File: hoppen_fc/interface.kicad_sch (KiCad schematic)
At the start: 56 parts, among them J10 XH2.5-3P, J11 XH2.5-3P, J12 GH1.25-4P, J13 GH1.25-4P, J14 XH2.5-3P, J15 GH1.25-4P, J16 GH1.25-2P, J17 GH1.25-2P, J18 GH1.25-5P, J3 GH1.25-4P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

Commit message: work
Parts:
- removed C98: 100n, 0_resistor_smd:R_0603_1608Metric, symbol Device:C
- removed J14: XH2.5-3P, symbol 0_connectors:Conn_01x03_Mounting
- removed R54, R55, R57, R60: 47k, symbol Device:R
- added C77: 100n, 0_capacitor_smd:C_0402_1005Metric, symbol Device:C
- added J2: PH2.0-3P, 0_connectors:S3B-PH-SM4-TB-LF-SN, symbol 0_connectors:Conn_01x03_Mounting
- added R13, R14, R15, R20: 47k, 0_resistor_smd:R_0402_1005Metric, symbol Device:R
- C68, C69, C82, C83, C85, C87, C89, C91, C92, C93, C95, C96, C97: footprint 0_resistor_smd:R_0603_1608Metric -> 0_capacitor_smd:C_0402_1005Metric
- C86, C88, C90, C94: footprint (none) -> 0_capacitor_smd:CASE-B-3528-21; LCSC (none) -> C7199
- J10, J11, J6, J9: value XH2.5-3P -> PH2.0-3P; footprint (none) -> 0_connectors:S3B-PH-SM4-TB-LF-SN
- J12, J13, J15, J3, J5: footprint (none) -> 0_connectors:SM04B-GHS-TB-LF-SN
- J16, J17: footprint (none) -> 0_connectors:SM02B-GHS-TB-LF-SN
- J18: footprint (none) -> 0_connectors:SM05B-GHS-TB-LF-SN
- J7: footprint (none) -> 0_connectors:SM08B-GHS-TB-LF-SN
- J8: footprint (none) -> 0_connectors:SM06B-GHS-TB-LF-SN
- JP3, JP4: footprint (none) -> 0_misc:SolderJumper-2_P1.3mm_Bridged_RoundedPad1.0x1.5mm
- R56, R61, R62: footprint (none) -> 0_resistor_smd:R_0402_1005Metric
- U15: footprint (none) -> 0_power:SOT-23-5_L3.0-W1.7-P0.95-LS2.8-BL
- U16: footprint Package_TO_SOT_SMD:SOT-353_SC-70-5 -> 0_transceivers:SOT-23-5
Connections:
- net +3V3: now also C97.1
- net +5V_EXT: now also J11.1 (Pin_1)
- net +BAT: now also C77.1, J2.1 (Pin_1); no longer C89.1, J11.1 (Pin_1)
- net CAM_PWR: now also C89.1; no longer C97.1
- net EXT_LED_D_5V: now also J11.2 (Pin_2)
- net GND: now also C77.2, J2.3 (Pin_3), J2.MP1, J2.MP2, R13.2, R14.2, R15.2, R20.2
- net PWM2: now also J2.2 (Pin_2), R15.1; no longer J9.2 (Pin_2)
- net PWM3: now also J9.2 (Pin_2), R14.1; no longer J10.2 (Pin_2)
- net PWM4: now also J10.2 (Pin_2), R13.1; no longer J11.2 (Pin_2)
- net at U15.3 (RSET): now also R20.1

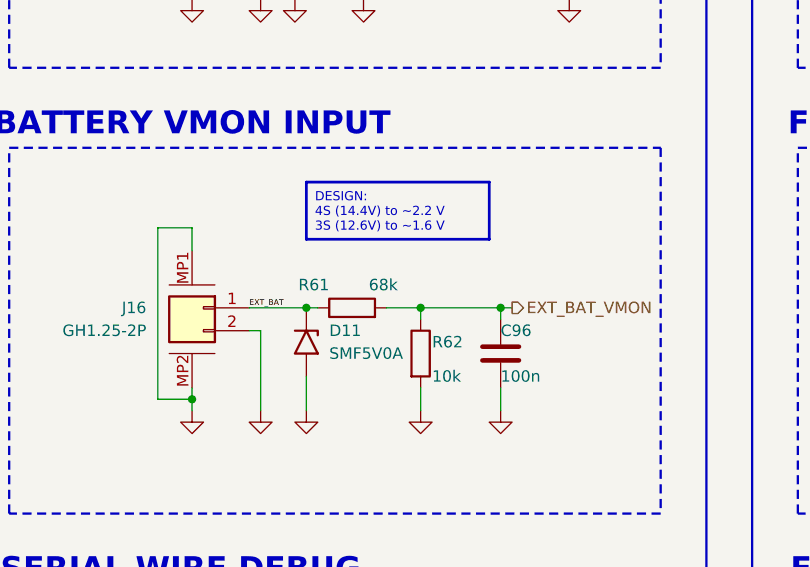
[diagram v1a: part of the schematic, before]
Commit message: power input/generation reworked
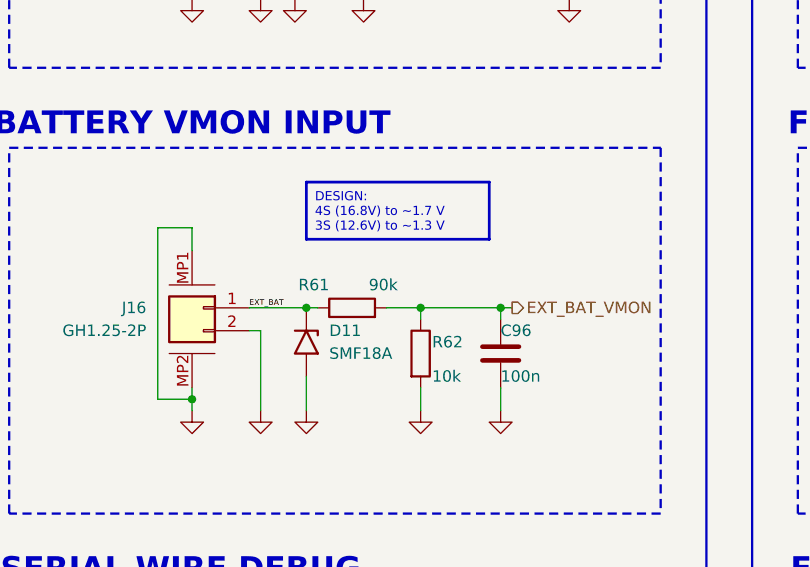
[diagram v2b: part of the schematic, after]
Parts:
- removed D11: SMF5V0A, 0_diodes:D_SMF, symbol 0_diodes:SMF5V0A
- added D11: SMF18A, Diode_SMD:D_SMF, symbol Diode:SMF18A
- C84: footprint (none) -> 0_capacitor_smd:CASE-B-3528-21; LCSC (none) -> C7199
- R61: value 68k -> 90k
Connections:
- net EXT_BAT: now also D11.1 (A1)
- net GND: now also D11.2 (A2)
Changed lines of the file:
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@@
 		)
 	)
-	(text_box "DESIGN:\n4S (14.4V) to ~2.2 V\n3S (12.6V) to ~1.6 V"
+	(text_box "DESIGN:\n4S (16.8V) to ~1.7 V\n3S (12.6V) to ~1.3 V"
 		(exclude_from_sim no)
 		(at 247.65 104.14 0)
@@
 	)
 	(junction
-		(at 247.65 118.11)
-		(diameter 0)
-		(color 0 0 0 0)
-	)
-	(junction
 		(at 148.59 133.35)
 		(diameter 0)
@@
 	)
 	(junction
+		(at 247.65 118.11)
+		(diameter 0)
+		(color 0 0 0 0)
+	)
+	(junction
 		(at 246.38 217.17)
 		(diameter 0)
@@
 	(wire
 		(pts
-			(xy 241.3 118.11) (xy 247.65 118.11)
-		)
-		(stroke
-			(width 0)
-			(type default)
-		)
-	)
-	(wire
-		(pts
 			(xy 242.57 207.01) (xy 242.57 219.71)
 		)
@@
 	(wire
 		(pts
+			(xy 247.65 118.11) (xy 248.92 118.11)
+		)
+		(stroke
+			(width 0)
+			(type default)
+		)
+	)
+	(wire
+		(pts
 			(xy 330.2 168.91) (xy 330.2 158.75)
 		)
@@
 	(wire
 		(pts
-			(xy 247.65 118.11) (xy 248.92 118.11)
+			(xy 241.3 118.11) (xy 247.65 118.11)
 		)
 		(stroke
@@
 			)
 		)
-		(property "Value" "68k"
+		(property "Value" "90k"
 			(at 257.81 115.57 90)
 			(effects
@@
 	)
 	(symbol
-		(lib_id "power:GND")
-		(at 167.64 134.62 0)
+		(lib_id "Diode:SMF18A")
+		(at 247.65 121.92 270)
 		(unit 1)
 		(exclude_from_sim no)
@@
 		(dnp no)
 		(fields_autoplaced yes)
-		(property "Reference" "#PWR0174"
-			(at 167.64 140.97 0)
+		(property "Reference" "D11"
+			(at 250.19 120.6499 90)
 			(effects
 				(font
 					(size 1.27 1.27)
 				)
-				(hide yes)
+				(justify left)
 			)
 		)
-		(property "Value" "GND"
-			(at 167.64 139.7 0)
+		(property "Value" "SMF18A"
+			(at 250.19 123.1899 90)
 			(effects
 				(font
 					(size 1.27 1.27)
 				)
-				(hide yes)
+				(justify left)
 			)
 		)
-		(property "Footprint" ""
-			(at 167.64 134.62 0)
+		(property "Footprint" "Diode_SMD:D_SMF"
+			(at 242.57 121.92 0)
 			(effects
 				(font
@@
 			)
 		)
-		(property "Datasheet" ""
-			(at 167.64 134.62 0)
+		(property "Datasheet" "https://www.vishay.com/doc?85881"
+			(at 247.65 120.65 0)
 			(effects
 				(font
@@
 			)
 		)
-		(property "Description" "Power symbol creates a global label with name \"GND\" , ground"
-			(at 167.64 134.62 0)
+		(property "Description" "200W unidirectional Transil Transient Voltage Suppressor, 18Vrwm, SMF"
+			(at 247.65 121.92 0)
 			(effects
 				(font
@@
 			)
 		)
+		(pin "2"
+		)
 		(pin "1"
 		)
 		(instances
-			(project "hoppen_fc"
+			(project ""
 				(path "/abe950a1-9eef-4508-9fd4-31d3e723e029/c85454e5-a89e-41eb-a5ed-71b4fc4cf13a/1b965b44-1377-4308-8bb4-a6ed39c8528f"
-					(reference "#PWR0174")
+					(reference "D11")
 					(unit 1)
 				)
@@
 	)
 	(symbol
-		(lib_id "power:+3.3V")
-		(at 67.31 107.95 0)
+		(lib_id "power:GND")
+		(at 167.64 134.62 0)
 		(unit 1)
 		(exclude_from_sim no)
@@
 		(dnp no)
 		(fields_autoplaced yes)
-		(property "Reference" "#PWR0116"
-			(at 67.31 111.76 0)
+		(property "Reference" "#PWR0174"
+			(at 167.64 140.97 0)
 			(effects
 				(font
@@
 			)
 		)
-		(property "Value" "+5V"
-			(at 67.31 102.87 0)
+		(property "Value" "GND"
+			(at 167.64 139.7 0)
 			(effects
 				(font
 					(size 1.27 1.27)
 				)
+				(hide yes)
 			)
 		)
 		(property "Footprint" ""
-			(at 67.31 107.95 0)
+			(at 167.64 134.62 0)
 			(effects
 				(font
@@
 		)
 		(property "Datasheet" ""
-			(at 67.31 107.95 0)
+			(at 167.64 134.62 0)
 			(effects
 				(font
@@
 			)
 		)
-		(property "Description" "Power symbol creates a global label with name \"+3.3V\""
-			(at 67.31 107.95 0)
+		(property "Description" "Power symbol creates a global label with name \"GND\" , ground"
+			(at 167.64 134.62 0)
 			(effects
 				(font
@@
 			(project "hoppen_fc"
 				(path "/abe950a1-9eef-4508-9fd4-31d3e723e029/c85454e5-a89e-41eb-a5ed-71b4fc4cf13a/1b965b44-1377-4308-8bb4-a6ed39c8528f"
-					(reference "#PWR0116")
+					(reference "#PWR0174")
 					(unit 1)
 				)
@@
 	)
 	(symbol
-		(lib_id "power:GND")
-		(at 260.35 129.54 0)
+		(lib_id "power:+3.3V")
+		(at 67.31 107.95 0)
 		(unit 1)
 		(exclude_from_sim no)
@@
 		(dnp no)
 		(fields_autoplaced yes)
-		(property "Reference" "#PWR0194"
-			(at 260.35 135.89 0)
+		(property "Reference" "#PWR0116"
+			(at 67.31 111.76 0)
 			(effects
 				(font
@@
 			)
 		)
-		(property "Value" "GND"
-			(at 260.35 134.62 0)
+		(property "Value" "+5V"
+			(at 67.31 102.87 0)
 			(effects
 				(font
 					(size 1.27 1.27)
 				)
-				(hide yes)
 			)
 		)
 		(property "Footprint" ""
-			(at 260.35 129.54 0)
+			(at 67.31 107.95 0)
 			(effects
 				(font
@@
 		)
 		(property "Datasheet" ""
-			(at 260.35 129.54 0)
+			(at 67.31 107.95 0)
 			(effects
 				(font
@@
 			)
 		)
-		(property "Description" "Power symbol creates a global label with name \"GND\" , ground"
-			(at 260.35 129.54 0)
+		(property "Description" "Power symbol creates a global label with name \"+3.3V\""
+			(at 67.31 107.95 0)
 			(effects
 				(font
@@
 			(project "hoppen_fc"
 				(path "/abe950a1-9eef-4508-9fd4-31d3e723e029/c85454e5-a89e-41eb-a5ed-71b4fc4cf13a/1b965b44-1377-4308-8bb4-a6ed39c8528f"
-					(reference "#PWR0194")
+					(reference "#PWR0116")
 					(unit 1)
 				)
@@
 	(symbol
 		(lib_id "power:GND")
-		(at 71.12 167.64 0)
+		(at 260.35 129.54 0)
 		(unit 1)
 		(exclude_from_sim no)
@@
 		(dnp no)
 		(fields_autoplaced yes)
-		(property "Reference" "#PWR0147"
-			(at 71.12 173.99 0)
+		(property "Reference" "#PWR0194"
+			(at 260.35 135.89 0)
 			(effects
 				(font
@@
 		)
 		(property "Value" "GND"
-			(at 71.12 172.72 0)
+			(at 260.35 134.62 0)
 			(effects
 				(font
@@
 		)
 		(property "Footprint" ""
-			(at 71.12 167.64 0)
+			(at 260.35 129.54 0)
 			(effects
 				(font
@@
 		)
 		(property "Datasheet" ""
-			(at 71.12 167.64 0)
+			(at 260.35 129.54 0)
 			(effects
 				(font
@@
 		)
 		(property "Description" "Power symbol creates a global label with name \"GND\" , ground"
-			(at 71.12 167.64 0)
+			(at 260.35 129.54 0)
 			(effects
 				(font
@@
 			(project "hoppen_fc"
 				(path "/abe950a1-9eef-4508-9fd4-31d3e723e029/c85454e5-a89e-41eb-a5ed-71b4fc4cf13a/1b965b44-1377-4308-8bb4-a6ed39c8528f"
-					(reference "#PWR0147")
+					(reference "#PWR0194")
 					(unit 1)
 				)
@@
 	)
 	(symbol
-		(lib_id "0_diodes:SMF5V0A")
-		(at 247.65 121.92 270)
+		(lib_id "power:GND")
+		(at 71.12 167.64 0)
 		(unit 1)
 		(exclude_from_sim no)
@@
 		(dnp no)
 		(fields_autoplaced yes)
-		(property "Reference" "D11"
-			(at 250.19 120.6499 90)
+		(property "Reference" "#PWR0147"
+			(at 71.12 173.99 0)
 			(effects
 				(font
 					(size 1.27 1.27)
 				)
-				(justify left)
+				(hide yes)
 			)
 		)
-		(property "Value" "SMF5V0A"
-			(at 250.19 123.1899 90)
+		(property "Value" "GND"
+			(at 71.12 172.72 0)
 			(effects
 				(font
 					(size 1.27 1.27)
 				)
-				(justify left)
+				(hide yes)
 			)
 		)
-		(property "Footprint" "0_diodes:D_SMF"
-			(at 261.62 121.92 0)
+		(property "Footprint" ""
+			(at 71.12 167.64 0)
 			(effects
 				(font
@@
 			)
 		)
-		(property "Datasheet" "https://www.vishay.com/doc?85881"
-			(at 256.54 121.92 0)
+		(property "Datasheet" ""
+			(at 71.12 167.64 0)
 			(effects
 				(font
@@
 			)
 		)
-		(property "Description" "200W unidirectional Transil Transient Voltage Suppressor, 5Vrwm, SMF"
-			(at 259.08 121.92 0)
+		(property "Description" "Power symbol creates a global label with name \"GND\" , ground"
+			(at 71.12 167.64 0)
 			(effects
 				(font
@@
 			)
 		)
-		(pin "2"
-		)
 		(pin "1"
 		)
@@
 			(project "hoppen_fc"
 				(path "/abe950a1-9eef-4508-9fd4-31d3e723e029/c85454e5-a89e-41eb-a5ed-71b4fc4cf13a/1b965b44-1377-4308-8bb4-a6ed39c8528f"
-					(reference "D11")
+					(reference "#PWR0147")
 					(unit 1)
 				)
@@
 			)
 		)
-		(property "Footprint" ""
+		(property "Footprint" "0_capacitor_smd:CASE-B-3528-21"
 			(at 168.6052 67.31 0)
 			(effects
@@
 			(at 167.64 63.5 0)
 			(effects
+				(font
+					(size 1.27 1.27)
+				)
+				(hide yes)
+			)
+		)
+		(property "LCSC" "C7199"
+			(at 167.64 63.5 0)
+			(effects

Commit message: finished routing, starting doublechecking and componenting
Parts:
- removed C84, C86, C88, C90: 22u, 0_capacitor_smd:CASE-B-3528-21, symbol Device:C_Polarized
- added C55, C56, C58, C59, C60, C61, C62, C63: 10u, 0_capacitor_smd:C_0805_2012Metric, symbol Device:C
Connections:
- net GND: now also C55.2, C56.2, C58.2, C59.2, C60.2, C61.2, C62.2, C63.2
- net +BAT renamed +BAT_PROT
- net +BAT_PROT: now also C55.1, C56.1, C58.1, C59.1, C60.1, C61.1, C62.1, C63.1
